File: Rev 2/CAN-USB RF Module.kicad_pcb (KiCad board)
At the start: 4 copper layers, 72 x 47.2 mm, 78 parts, among them IC1 ESDALC6V1W5, J1 Conn_02x05_Top_Bottom, J2 Fuel Cell Connector, J3 USB JMPR, J4 USB_B_Micro, J5 Conn_Coaxial, J6 Conn_01x09_Socket, Q1 NMOS, SW1 RESET, SW2 BOOT0, U1 8MHz, U10 MCP2542FD-E/SN, U2 STM32L442KCU6, U3 TPS2596, U4 BAT54CTA, U5 AZ1117-3.3, U6 AZ1117-5.0, U7 FT234XD-R

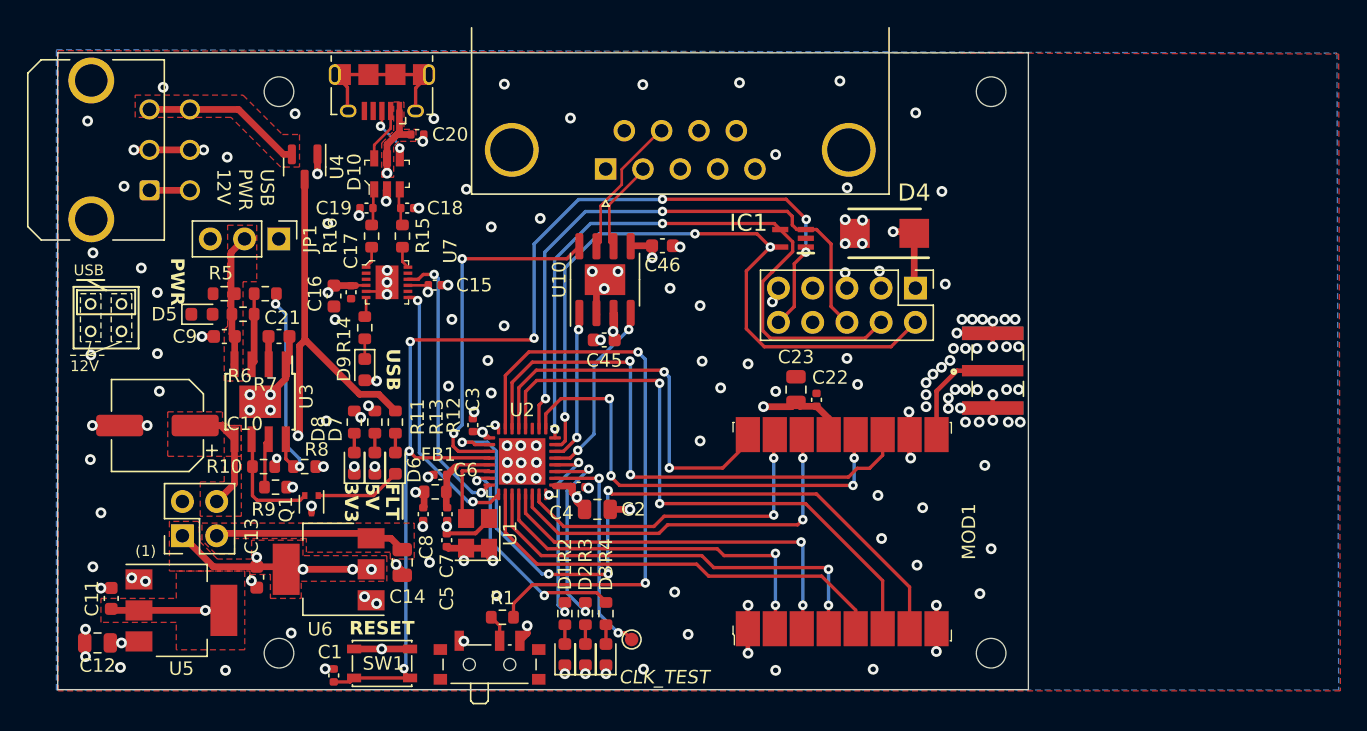
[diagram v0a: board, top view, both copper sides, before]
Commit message: added GPSW and HW DB
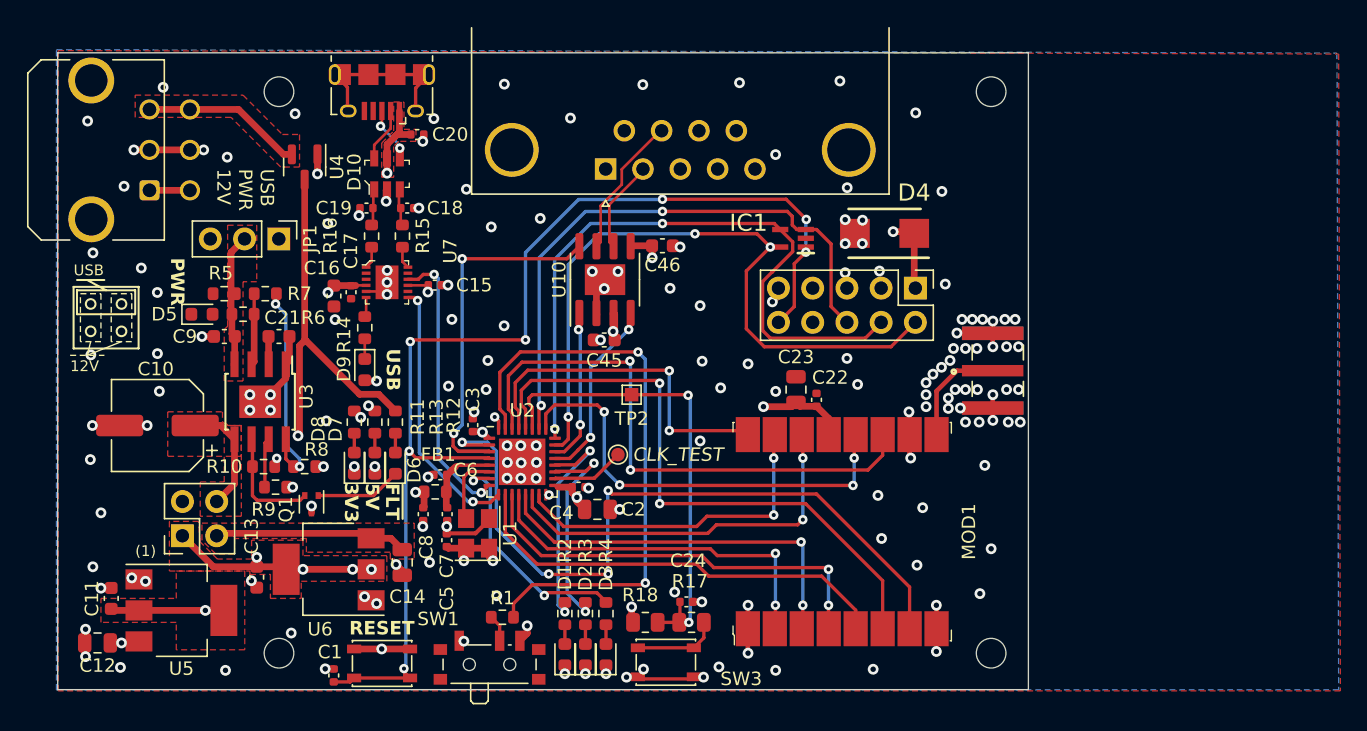
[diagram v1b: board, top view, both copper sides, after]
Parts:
- added C24: 100n, Capacitor_SMD:C_0402_1005Metric, F.Cu at (144.8, 111.8)
- added R17: 1k, Resistor_SMD:R_0805_2012Metric, F.Cu at (145.2, 113.3)
- added R18: 10k, Resistor_SMD:R_0805_2012Metric, F.Cu at (141.7, 113.3)
- added SW3: GPSW, Button_Switch_SMD:SW_SPST_PTS810, F.Cu at (143.3, 116.2)
- added TP2: GPIO, TestPoint:TestPoint_Pad_1.0x1.0mm, F.Cu at (140.7, 96.4)
- U2: value STM32L442KCU6 -> STM32L432KBU6
- moved TP1 13.8 mm to (139.7, 100.8)
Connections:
- U2 pad 27: /SW_RXTX -> Net-(U2-PB4)
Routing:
- net Net-(U2-PB4): track 0.00 -> 35.2 mm, vias 0 -> 2
- net Net-(U2-PA8): track 16.5 -> 5.41 mm, vias 2 -> 0
- net GND: track 72.4 -> 79.0 mm, vias 167 -> 170
- net Net-(R17-Pad1): track 0.00 -> 6.34 mm
- net +3V3: track 182.7 -> 187.4 mm, vias 13 -> 14
- net /DIO2: track 28.9 -> 25.8 mm
- net Net-(U2-PA10): track 14.4 -> 16.9 mm
- net /CAN_STBY: track 26.1 -> 28.4 mm
- net +3.3VA: track 5.97 -> 7.85 mm
- net /DIO4: track 34.2 -> 33.0 mm
- net Net-(U2-PA9): track 15.1 -> 16.2 mm
- net /BOOT0: track 43.3 -> 44.0 mm
- net /SX_RESET: track 44.5 -> 45.1 mm
- net Net-(U2-PA1): track 17.1 -> 17.6 mm

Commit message: Thats it no more changes
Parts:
- moved G*** 24.7 mm to (163.6, 110.2)
- moved J5 4.19 mm to (167.5, 98.8)
- moved R1 0.13 mm to (131.1, 112.8)
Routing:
- net GND: track 79.0 -> 93.2 mm, vias 170 -> 192
- net Net-(J5-In): track 8.02 -> 4.39 mm
- net +3V3: track 187.4 -> 184.8 mm
- net /CAN_STBY: track 28.4 -> 26.6 mm
- net Net-(D5-A): track 0.00 -> 1.54 mm
- net Net-(R10-Pad1): track 31.1 -> 32.4 mm
- net /Power Regulator/~{FAULT}: track 9.03 -> 8.38 mm
- net Net-(U2-PB4): track 35.2 -> 35.8 mm
- net /DEBUG_SWDIO: track 52.1 -> 52.5 mm, vias 3 -> 2
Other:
- board text added: "(2)"
- board text added: "(3)"
- board text added: "(4)"
- board text removed: "12V"
